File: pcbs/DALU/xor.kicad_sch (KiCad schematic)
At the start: 3 parts, among them U601 74HC86, U602 74HC86, U603 74HC245

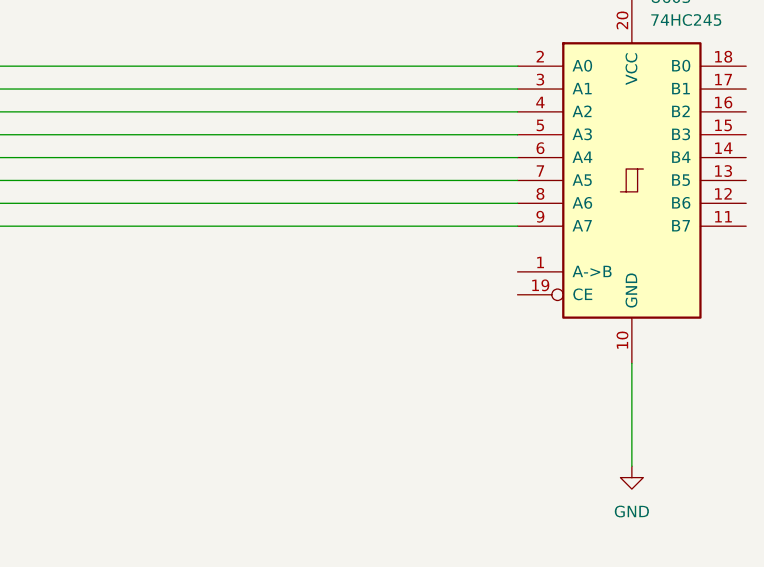
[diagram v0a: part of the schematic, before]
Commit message: Starting to do the routing. Schematic not yet complete, though
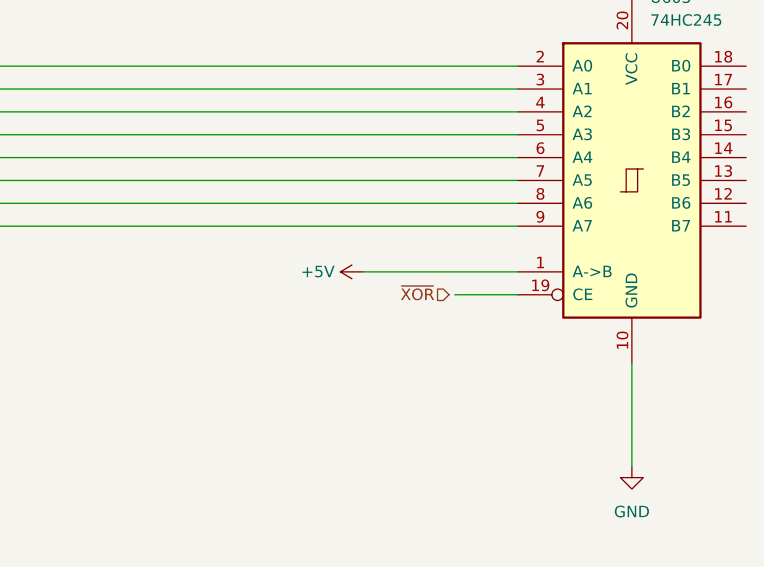
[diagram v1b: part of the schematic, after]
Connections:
- net +5V: now also U603.1 (A->B)
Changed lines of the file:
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@@
+    (stroke (width 0) (type default) (color 0 0 0 0))
+  )
+  (wire (pts (xy 186.055 67.31) (xy 203.2 67.31))
     (stroke (width 0) (type default) (color 0 0 0 0))
   )
@@
     (stroke (width 0) (type default) (color 0 0 0 0))
   )
+  (wire (pts (xy 196.215 69.85) (xy 203.2 69.85))
+    (stroke (width 0) (type default) (color 0 0 0 0))
+  )
   (wire (pts (xy 125.73 86.36) (xy 125.73 52.07))
     (stroke (width 0) (type default) (color 0 0 0 0))
@@
   )
   (hierarchical_label "A[0..7]" (shape input) (at 38.1 25.4 180)
+    (effects (font (size 1.27 1.27)) (justify right))
+  )
+  (hierarchical_label "~{XOR}" (shape input) (at 195.58 69.85 180)
     (effects (font (size 1.27 1.27)) (justify right))
   )
@@
     (pin "7")
   )
+  (symbol (lib_id "power:+5V") (at 186.055 67.31 90) (unit 1)
+    (in_bom yes) (on_board yes) (fields_autoplaced)
+    (property "Reference" "#PWR0102" (id 0) (at 189.865 67.31 0)
+      (effects (font (size 1.27 1.27)) hide)
+    )
+    (property "Value" "+5V" (id 1) (at 182.88 67.3099 90)
+      (effects (font (size 1.27 1.27)) (justify left))
+    )
+    (property "Footprint" "" (id 2) (at 186.055 67.31 0)
+      (effects (font (size 1.27 1.27)) hide)
+    )
+    (property "Datasheet" "" (id 3) (at 186.055 67.31 0)
+      (effects (font (size 1.27 1.27)) hide)
+    )
+    (pin "1")
+  )
   (symbol (lib_id "74xx:74HC245") (at 215.9 57.15 0) (unit 1)

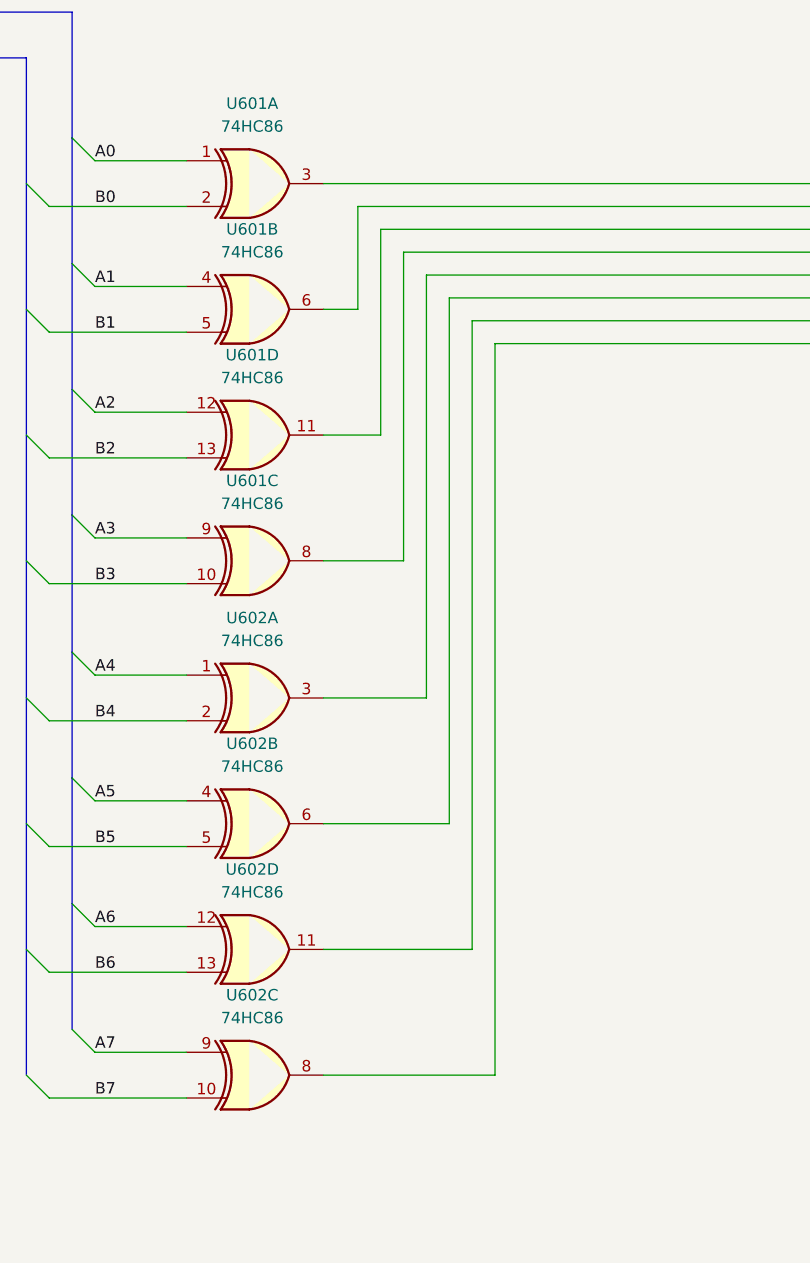
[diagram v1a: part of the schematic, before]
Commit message: Routing the XOR
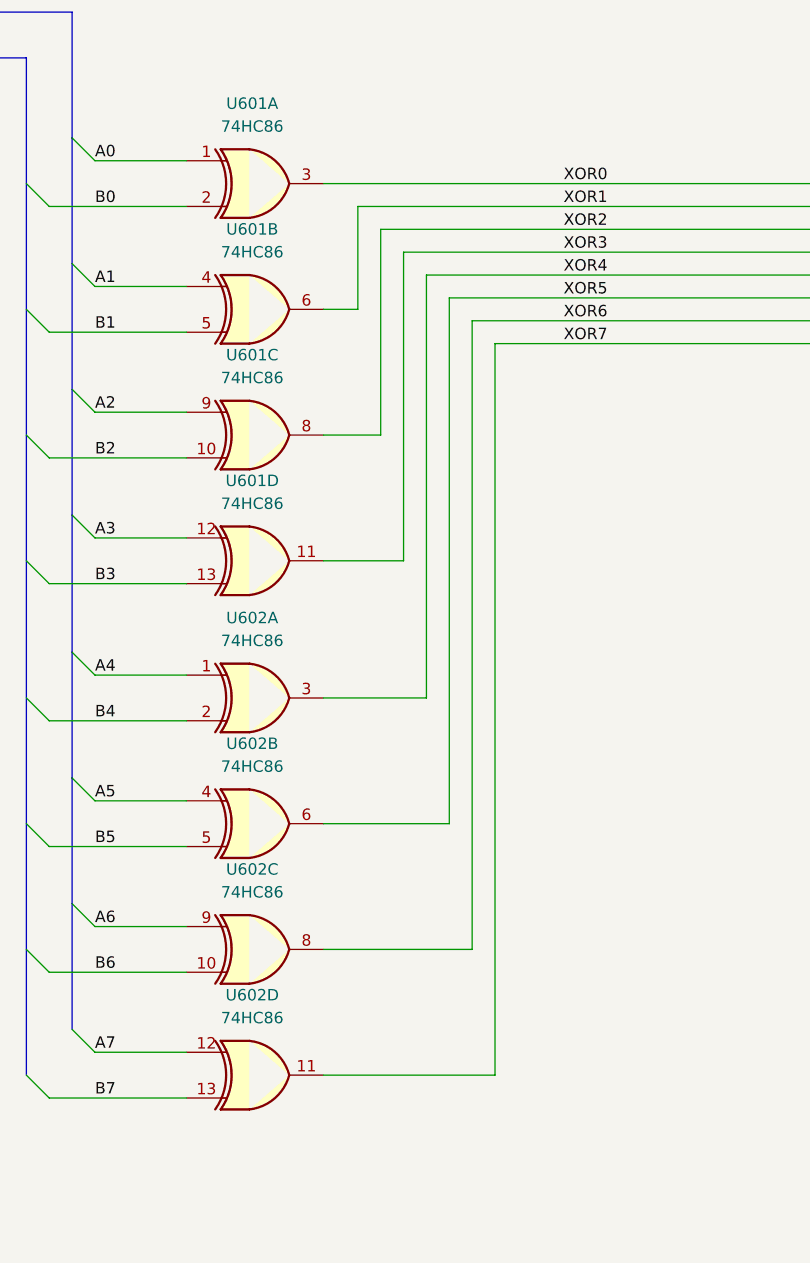
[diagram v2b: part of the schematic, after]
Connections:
- net A2: now also U601.9; no longer U601.12
- net A3: now also U601.12; no longer U601.9
- net A6: now also U602.9; no longer U602.12
- net A7: now also U602.12; no longer U602.9
- net B2: now also U601.10; no longer U601.13
- net B3: now also U601.13; no longer U601.10
- net B6: now also U602.10; no longer U602.13
- net B7: now also U602.13; no longer U602.10
- net XOR0: now reaches U601.3, U603.2 (A0)
- net XOR5: now reaches U602.6, U603.7 (A5)
- net XOR6: now reaches U602.8
- net XOR6: now also U603.8 (A6); no longer U603.9 (A7)
- net XOR2: now reaches U601.8
- net XOR2: now also U603.4 (A2); no longer U603.5 (A3)
- net XOR7: now reaches U602.11
- net XOR7: now also U603.9 (A7); no longer U603.8 (A6)
- net XOR4: now reaches U602.3, U603.6 (A4)
- net XOR3: now reaches U601.11
- net XOR3: now also U603.5 (A3); no longer U603.4 (A2)
- net XOR1: now reaches U601.6, U603.3 (A1)
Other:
- moved on the sheet: U601C, U601D, U602C, U602D
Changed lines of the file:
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@@
     (stroke (width 0) (type default) (color 0 0 0 0))
   )
+  (label "XOR5" (at 143.51 57.15 0)
+    (effects (font (size 1.27 1.27)) (justify left bottom))
+  )
+  (label "XOR0" (at 143.51 44.45 0)
+    (effects (font (size 1.27 1.27)) (justify left bottom))
+  )
+  (label "XOR3" (at 143.51 52.07 0)
+    (effects (font (size 1.27 1.27)) (justify left bottom))
+  )
   (label "A2" (at 91.44 69.85 0)
     (effects (font (size 1.27 1.27)) (justify left bottom))
   )
+  (label "XOR4" (at 143.51 54.61 0)
+    (effects (font (size 1.27 1.27)) (justify left bottom))
+  )
   (label "B1" (at 91.44 60.96 0)
     (effects (font (size 1.27 1.27)) (justify left bottom))
@@
   )
   (label "B4" (at 91.44 104.14 0)
+    (effects (font (size 1.27 1.27)) (justify left bottom))
+  )
+  (label "XOR1" (at 143.51 46.99 0)
+    (effects (font (size 1.27 1.27)) (justify left bottom))
+  )
+  (label "XOR2" (at 143.51 49.53 0)
+    (effects (font (size 1.27 1.27)) (justify left bottom))
+  )
+  (label "XOR7" (at 143.51 62.23 0)
+    (effects (font (size 1.27 1.27)) (justify left bottom))
+  )
+  (label "XOR6" (at 143.51 59.69 0)
     (effects (font (size 1.27 1.27)) (justify left bottom))
   )
@@
     (pin "7")
   )
-  (symbol (lib_id "74xx:74HC86") (at 109.22 143.51 0) (unit 3)
+  (symbol (lib_id "74xx:74HC86") (at 109.22 129.54 0) (unit 3)
+    (in_bom yes) (on_board yes) (fields_autoplaced)
+    (property "Reference" "U602" (id 0) (at 108.9152 120.65 0))
+    (property "Value" "74HC86" (id 1) (at 108.9152 123.19 0))
+    (property "Footprint" "Package_DIP:DIP-14_W7.62mm_Socket" (id 2) (at 109.22 129.54 0)
+      (effects (font (size 1.27 1.27)) hide)
+    )
+    (property "Datasheet" "http://www.ti.com/lit/gpn/sn74HC86" (id 3) (at 109.22 129.54 0)
+      (effects (font (size 1.27 1.27)) hide)
+    )
+    (pin "1")
+    (pin "2")
+    (pin "3")
+    (pin "4")
+    (pin "5")
+    (pin "6")
+    (pin "10")
+    (pin "8")
+    (pin "9")
+    (pin "11")
+    (pin "12")
+    (pin "13")
+    (pin "14")
+    (pin "7")
+  )
+  (symbol (lib_id "74xx:74HC86") (at 109.22 72.39 0) (unit 3)
+    (in_bom yes) (on_board yes) (fields_autoplaced)
+    (property "Reference" "U601" (id 0) (at 108.9152 63.5 0))
+    (property "Value" "74HC86" (id 1) (at 108.9152 66.04 0))
+    (property "Footprint" "Package_DIP:DIP-14_W7.62mm_Socket" (id 2) (at 109.22 72.39 0)
+      (effects (font (size 1.27 1.27)) hide)
+    )
+    (property "Datasheet" "http://www.ti.com/lit/gpn/sn74HC86" (id 3) (at 109.22 72.39 0)
+      (effects (font (size 1.27 1.27)) hide)
+    )
+    (pin "1")
+    (pin "2")
+    (pin "3")
+    (pin "4")
+    (pin "5")
+    (pin "6")
+    (pin "10")
+    (pin "8")
+    (pin "9")
+    (pin "11")
+    (pin "12")
+    (pin "13")
+    (pin "14")
+    (pin "7")
+  )
+  (symbol (lib_id "power:GND") (at 57.15 186.69 0) (unit 1)
+    (in_bom yes) (on_board yes) (fields_autoplaced)
+    (property "Reference" "#PWR0604" (id 0) (at 57.15 193.04 0)
+      (effects (font (size 1.27 1.27)) hide)
+    )
+    (property "Value" "GND" (id 1) (at 57.15 191.77 0))
+    (property "Footprint" "" (id 2) (at 57.15 186.69 0)
+      (effects (font (size 1.27 1.27)) hide)
+    )
+    (property "Datasheet" "" (id 3) (at 57.15 186.69 0)
+      (effects (font (size 1.27 1.27)) hide)
+    )
+    (pin "1")
+  )
+  (symbol (lib_id "power:GND") (at 29.21 186.69 0) (unit 1)
+    (in_bom yes) (on_board yes) (fields_autoplaced)
+    (property "Reference" "#PWR0602" (id 0) (at 29.21 193.04 0)
+      (effects (font (size 1.27 1.27)) hide)
+    )
+    (property "Value" "GND" (id 1) (at 29.21 191.77 0))
+    (property "Footprint" "" (id 2) (at 29.21 186.69 0)
+      (effects (font (size 1.27 1.27)) hide)
+    )
+    (property "Datasheet" "" (id 3) (at 29.21 186.69 0)
+      (effects (font (size 1.27 1.27)) hide)
+    )
+    (pin "1")
+  )
+  (symbol (lib_id "power:+5V") (at 29.21 156.21 0) (unit 1)
+    (in_bom yes) (on_board yes) (fields_autoplaced)
+    (property "Reference" "#PWR0601" (id 0) (at 29.21 160.02 0)
+      (effects (font (size 1.27 1.27)) hide)
+    )
+    (property "Value" "+5V" (id 1) (at 29.21 151.13 0))
+    (property "Footprint" "" (id 2) (at 29.21 156.21 0)
+      (effects (font (size 1.27 1.27)) hide)
+    )
+    (property "Datasheet" "" (id 3) (at 29.21 156.21 0)
+      (effects (font (size 1.27 1.27)) hide)
+    )
+    (pin "1")
+  )
+  (symbol (lib_id "74xx:74HC86") (at 109.22 143.51 0) (unit 4)
     (in_bom yes) (on_board yes) (fields_autoplaced)
     (property "Reference" "U602" (id 0) (at 108.9152 134.62 0))
@@
     (pin "7")
   )
-  (symbol (lib_id "74xx:74HC86") (at 109.22 86.36 0) (unit 3)
+  (symbol (lib_id "74xx:74HC86") (at 109.22 101.6 0) (unit 1)
+    (in_bom yes) (on_board yes) (fields_autoplaced)
+    (property "Reference" "U602" (id 0) (at 108.9152 92.71 0))
+    (property "Value" "74HC86" (id 1) (at 108.9152 95.25 0))
+    (property "Footprint" "Package_DIP:DIP-14_W7.62mm_Socket" (id 2) (at 109.22 101.6 0)
+      (effects (font (size 1.27 1.27)) hide)
+    )
+    (property "Datasheet" "http://www.ti.com/lit/gpn/sn74HC86" (id 3) (at 109.22 101.6 0)
+      (effects (font (size 1.27 1.27)) hide)
+    )
+    (pin "1")
+    (pin "2")
+    (pin "3")
+    (pin "4")
+    (pin "5")
+    (pin "6")
+    (pin "10")
+    (pin "8")
+    (pin "9")
+    (pin "11")
+    (pin "12")
+    (pin "13")
+    (pin "14")
+    (pin "7")
+  )
+  (symbol (lib_id "74xx:74HC86") (at 109.22 86.36 0) (unit 4)
     (in_bom yes) (on_board yes) (fields_autoplaced)
     (property "Reference" "U601" (id 0) (at 108.9152 77.47 0))
@@
       (effects (font (size 1.27 1.27)) hide)
     )
-    (pin "1")
-    (pin "2")
-    (pin "3")
-    (pin "4")
-    (pin "5")
-    (pin "6")
-    (pin "10")
-    (pin "8")
-    (pin "9")
-    (pin "11")
-    (pin "12")
-    (pin "13")
-    (pin "14")
-    (pin "7")
-  )
-  (symbol (lib_id "power:GND") (at 57.15 186.69 0) (unit 1)
-    (in_bom yes) (on_board yes) (fields_autoplaced)
-    (property "Reference" "#PWR0604" (id 0) (at 57.15 193.04 0)
-      (effects (font (size 1.27 1.27)) hide)
-    )
-    (property "Value" "GND" (id 1) (at 57.15 191.77 0))
-    (property "Footprint" "" (id 2) (at 57.15 186.69 0)
-      (effects (font (size 1.27 1.27)) hide)
-    )
-    (property "Datasheet" "" (id 3) (at 57.15 186.69 0)
-      (effects (font (size 1.27 1.27)) hide)
-    )
-    (pin "1")
-  )
-  (symbol (lib_id "power:GND") (at 29.21 186.69 0) (unit 1)
-    (in_bom yes) (on_board yes) (fields_autoplaced)
-    (property "Reference" "#PWR0602" (id 0) (at 29.21 193.04 0)
-      (effects (font (size 1.27 1.27)) hide)
-    )
-    (property "Value" "GND" (id 1) (at 29.21 191.77 0))
-    (property "Footprint" "" (id 2) (at 29.21 186.69 0)
-      (effects (font (size 1.27 1.27)) hide)
-    )
-    (property "Datasheet" "" (id 3) (at 29.21 186.69 0)
-      (effects (font (size 1.27 1.27)) hide)
-    )
-    (pin "1")
-  )
-  (symbol (lib_id "power:+5V") (at 29.21 156.21 0) (unit 1)
-    (in_bom yes) (on_board yes) (fields_autoplaced)
-    (property "Reference" "#PWR0601" (id 0) (at 29.21 160.02 0)
-      (effects (font (size 1.27 1.27)) hide)
-    )
-    (property "Value" "+5V" (id 1) (at 29.21 151.13 0))
-    (property "Footprint" "" (id 2) (at 29.21 156.21 0)
-      (effects (font (size 1.27 1.27)) hide)
-    )
-    (property "Datasheet" "" (id 3) (at 29.21 156.21 0)
-      (effects (font (size 1.27 1.27)) hide)
-    )
-    (pin "1")
-  )
-  (symbol (lib_id "74xx:74HC86") (at 109.22 129.54 0) (unit 4)
-    (in_bom yes) (on_board yes) (fields_autoplaced)
-    (property "Reference" "U602" (id 0) (at 108.9152 120.65 0))
-    (property "Value" "74HC86" (id 1) (at 108.9152 123.19 0))
-    (property "Footprint" "Package_DIP:DIP-14_W7.62mm_Socket" (id 2) (at 109.22 129.54 0)
-      (effects (font (size 1.27 1.27)) hide)
-    )
-    (property "Datasheet" "http://www.ti.com/lit/gpn/sn74HC86" (id 3) (at 109.22 129.54 0)
-      (effects (font (size 1.27 1.27)) hide)
-    )
-    (pin "1")
-    (pin "2")
-    (pin "3")
-    (pin "4")
-    (pin "5")
-    (pin "6")
-    (pin "10")
-    (pin "8")
-    (pin "9")
-    (pin "11")
-    (pin "12")
-    (pin "13")
-    (pin "14")
-    (pin "7")
-  )
-  (symbol (lib_id "74xx:74HC86") (at 109.22 101.6 0) (unit 1)
-    (in_bom yes) (on_board yes) (fields_autoplaced)
-    (property "Reference" "U602" (id 0) (at 108.9152 92.71 0))
-    (property "Value" "74HC86" (id 1) (at 108.9152 95.25 0))
-    (property "Footprint" "Package_DIP:DIP-14_W7.62mm_Socket" (id 2) (at 109.22 101.6 0)
-      (effects (font (size 1.27 1.27)) hide)
-    )
-    (property "Datasheet" "http://www.ti.com/lit/gpn/sn74HC86" (id 3) (at 109.22 101.6 0)
-      (effects (font (size 1.27 1.27)) hide)
-    )
-    (pin "1")
-    (pin "2")
-    (pin "3")
-    (pin "4")
-    (pin "5")
-    (pin "6")
-    (pin "10")
-    (pin "8")
-    (pin "9")
-    (pin "11")
-    (pin "12")
-    (pin "13")
-    (pin "14")
-    (pin "7")
-  )
-  (symbol (lib_id "74xx:74HC86") (at 109.22 72.39 0) (unit 4)
-    (in_bom yes) (on_board yes) (fields_autoplaced)
-    (property "Reference" "U601" (id 0) (at 108.9152 63.5 0))
-    (property "Value" "74HC86" (id 1) (at 108.9152 66.04 0))
-    (property "Footprint" "Package_DIP:DIP-14_W7.62mm_Socket" (id 2) (at 109.22 72.39 0)
-      (effects (font (size 1.27 1.27)) hide)
-    )
-    (property "Datasheet" "http://www.ti.com/lit/gpn/sn74HC86" (id 3) (at 109.22 72.39 0)
-      (effects (font (size 1.27 1.27)) hide)
-    )

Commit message: Fixing a lot of routing
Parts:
- added C601, C602, C603: 100n, Capacitor_SMD:C_0603_1608Metric, symbol Device:C
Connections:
- net +5V: now also C601.1, C602.1, C603.1
- net A0: now also U601.9; no longer U601.1
- net A1: now also U601.12; no longer U601.4
- net A2: now also U601.1; no longer U601.9
- net A3: now also U601.4; no longer U601.12
- net B0: now also U601.10; no longer U601.2
- net B1: now also U601.13; no longer U601.5
- net B2: now also U601.2; no longer U601.10
- net B3: now also U601.5; no longer U601.13
- net GND: now also C601.2, C602.2, C603.2
- net XOR0: now also U601.8; no longer U601.3
- net XOR1: now also U601.11; no longer U601.6
- net XOR2: now also U601.3; no longer U601.8
- net XOR3: now also U601.6; no longer U601.11
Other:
- moved on the sheet: U601A, U601B, U601C, U601D
